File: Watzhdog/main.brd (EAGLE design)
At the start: 100 x 80 mm, 42 parts, among them CN1 MICROUSB(MC-5F-02), IC1 C8051F381-GM, IC3 N25Q512A, IC6 MPU-9250, U1 MCP73831, U2 TPS61201

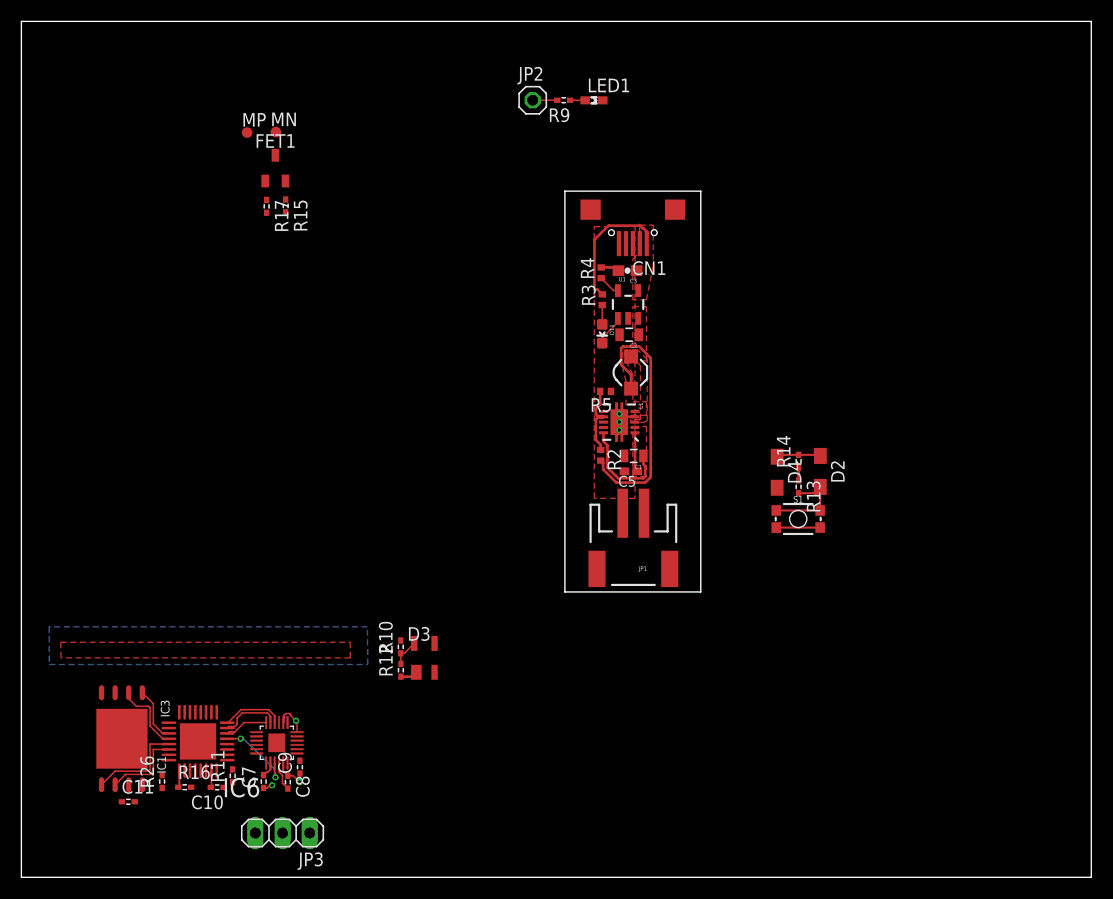
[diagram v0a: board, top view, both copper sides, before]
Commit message: Modified curcuit as a 2-layer board
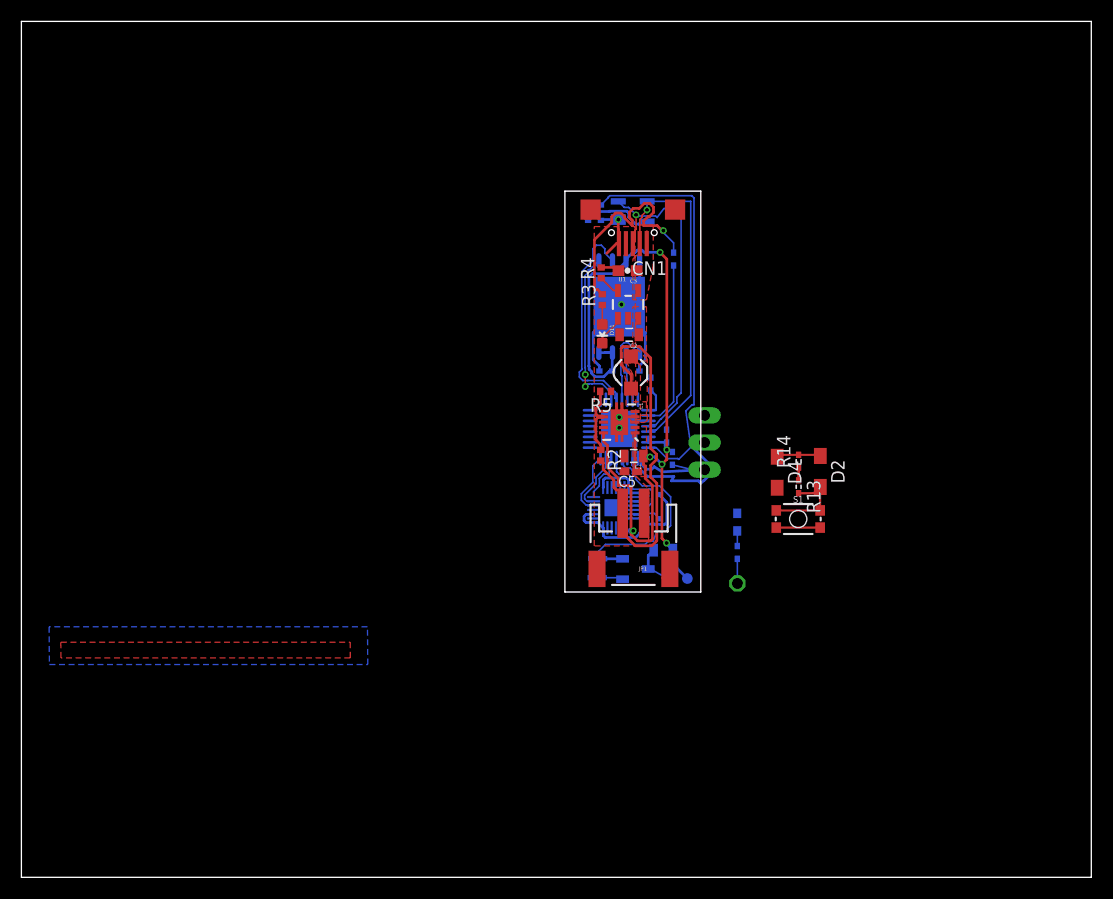
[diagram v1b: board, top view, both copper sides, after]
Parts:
- added C4: 22uF, CH_passive:0805
- added R1: 1k (Optional), reg,cap:1005
- moved IC3 61.6 mm to (55.9, 53.3), flipped to the bottom
- moved C11 60.1 mm to (54.6, 47.3), flipped to the bottom, turned to 180 degrees
- moved MP 58.6 mm to (62.2, 27.9), flipped to the bottom, turned to 90 degrees
- moved R26 58.4 mm to (57.2, 47.3), flipped to the bottom, turned to 0 degrees
- moved R16 57.6 mm to (58.8, 46.1), flipped to the bottom, turned to 90 degrees
- moved MN 55.5 mm to (60.3, 28.0), flipped to the bottom, turned to 90 degrees
- moved JP3 53.7 mm to (63.9, 40.6), flipped to the bottom, turned to 270 degrees
- moved C10 53.3 mm to (60.3, 41.2), flipped to the bottom, turned to 270 degrees
- moved R11 50.7 mm to (60.8, 39.2), flipped to the bottom
- moved FET1 50.4 mm to (57.4, 28.8), flipped to the bottom, turned to 90 degrees
- moved JP2 49.0 mm to (66.9, 27.5), flipped to the bottom, turned to 90 degrees
- moved IC1 49.0 mm to (55.9, 41.9), flipped to the bottom, turned to 0 degrees
- moved R17 46.5 mm to (53.8, 28.0), flipped to the bottom, turned to 0 degrees
- moved D3 46.0 mm to (57.1, 62.2), flipped to the bottom, turned to 90 degrees
- moved R12 45.8 mm to (53.6, 61.4), flipped to the bottom, turned to 0 degrees
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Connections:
- net N$10: now also C4.2
- net N$7: now also R1.P$1
- net VBUS: now also R1.P$2
- net VCC: now also C4.1
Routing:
- net VCC: track 12.4 -> 90.7 mm, vias 0 -> 6
- net DGND: track 14.5 -> 55.9 mm, vias 6 -> 4
- net N$18: track 0.00 -> 37.8 mm
- net D+: track 0.00 -> 32.0 mm, vias 0 -> 1
- net D-: track 0.00 -> 31.8 mm, vias 0 -> 1
- net PWM: track 0.00 -> 20.3 mm
- net VBUS: track 15.8 -> 33.6 mm, vias 0 -> 1
- net N$7: track 0.00 -> 15.6 mm
- net C2D: track 0.00 -> 14.3 mm
- net EEPROM_MISO: track 6.86 -> 20.0 mm
- net VBAT: track 28.7 -> 41.1 mm
- net EEPROM_!CS: track 5.17 -> 16.2 mm, vias 0 -> 2
- net C2CK: track 0.00 -> 9.38 mm
- net N$10: track 0.00 -> 3.95 mm
- net EEPROM_SCK: track 7.57 -> 4.41 mm
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
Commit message: Modified circuit
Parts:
- moved C10 0.33 mm to (60.6, 41.3)
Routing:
- net VBUS: track 33.6 -> 23.0 mm, vias 1 -> 2
- net VCC: track 90.7 -> 95.3 mm, vias 6 -> 7
- net DGND: track 55.9 -> 59.5 mm, vias 4 -> 5
- net D+: track 32.0 -> 29.9 mm, vias 1 -> 2
- net D-: track 31.8 -> 30.3 mm, vias 1 -> 3

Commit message: Modified circuit
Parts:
- moved C9 0.65 mm to (57.0, 32.2)
- moved C10 0.64 mm to (60.0, 41.3)
- moved C11 0.64 mm to (54.0, 47.3)
- moved C5 0.64 mm to (56.3, 37.9)
- moved C7 0.64 mm to (58.4, 35.8)
- moved IC1 0.64 mm to (55.2, 41.9)
- moved IC3 0.64 mm to (55.2, 53.3)
- moved L1 0.64 mm to (56.3, 47.2)
- moved R16 0.64 mm to (58.2, 46.1)
- moved U2 0.64 mm to (55.2, 42.5)
- moved C1 0.63 mm to (56.6, 39.4)
- moved C2 0.63 mm to (56.2, 50.7)
- moved C3 0.63 mm to (56.0, 56.7)
- moved C8 0.63 mm to (58.4, 33.5)
- moved D11 0.63 mm to (53.7, 50.8)
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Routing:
- net VBAT: track 41.4 -> 51.1 mm
- net VCC: track 95.3 -> 86.2 mm, vias 7 -> 8
- net DGND: track 59.5 -> 56.7 mm, vias 5 -> 7
- net PWM: track 20.0 -> 22.4 mm
- net C2CK: track 9.26 -> 10.5 mm
- net N$18: track 37.8 -> 39.0 mm
- net C2D: track 14.2 -> 14.9 mm

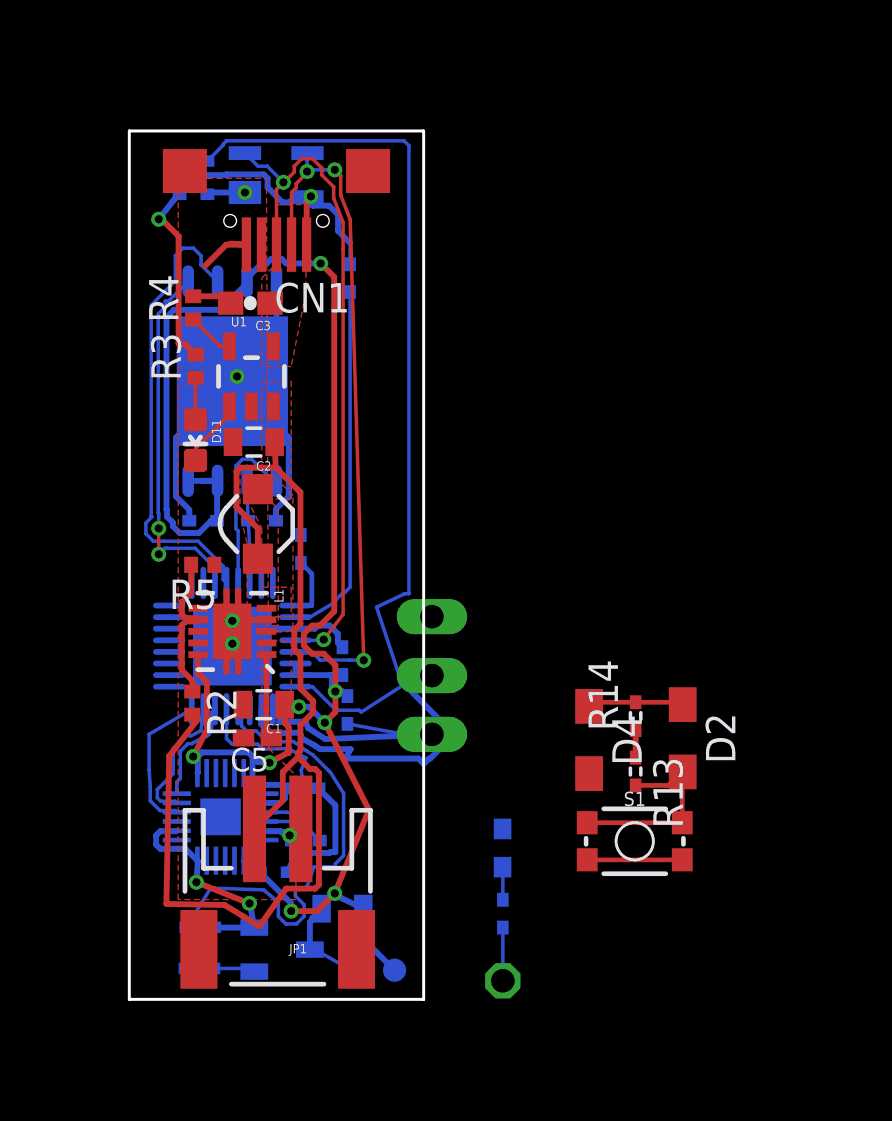
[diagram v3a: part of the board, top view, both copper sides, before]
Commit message: Modified parts position
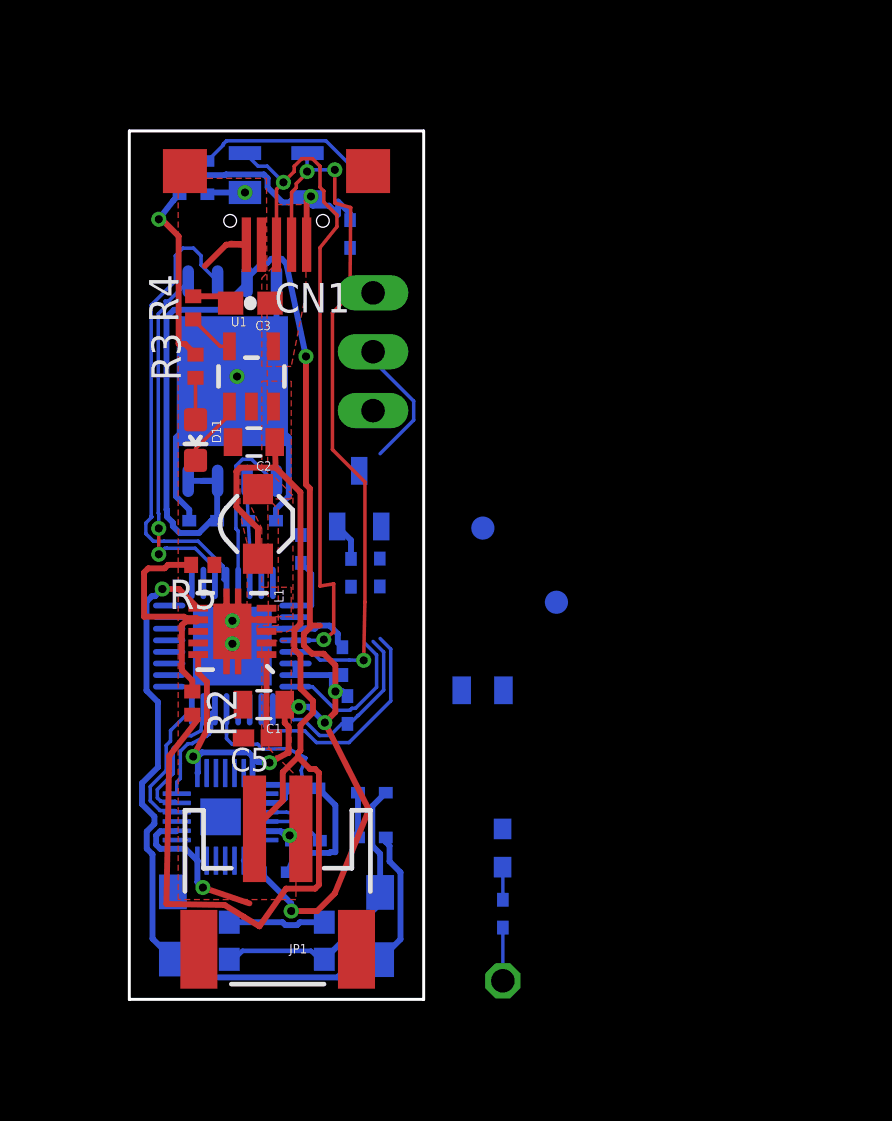
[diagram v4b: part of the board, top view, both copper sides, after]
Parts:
- removed C4: 22uF, CH_passive:0805
- added C6: 22uF, CH_passive:0805
- moved MN 19.9 mm to (66.1, 47.0)
- moved FET1 19.7 mm to (60.7, 48.3), turned to 0 degrees
- moved D4 19.7 mm to (52.7, 29.9), flipped to the bottom, turned to 90 degrees
- moved R17 18.8 mm to (61.6, 45.1), turned to 270 degrees
- moved MP 17.3 mm to (69.2, 43.8)
- moved R15 16.6 mm to (60.4, 45.1), turned to 270 degrees
- moved S1 16.0 mm to (57.2, 29.2), flipped to the bottom, turned to 180 degrees
- moved D2 15.4 mm to (61.6, 29.8), flipped to the bottom, turned to 90 degrees
- moved JP3 14.2 mm to (61.3, 54.6)
- moved R14 12.5 mm to (61.3, 33.7), flipped to the bottom, turned to 180 degrees
- moved R13 11.4 mm to (61.3, 35.6), flipped to the bottom, turned to 180 degrees
- moved R1 1.91 mm to (60.3, 59.7)
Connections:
- net DGND: now also C6.2
- net N$10: no longer C4.2
- net VCC: now also C6.1; no longer C4.1
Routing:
- net N$6: track 4.14 -> 35.0 mm, vias 0 -> 1
- net N$18: track 39.0 -> 14.3 mm
- net PWM: track 22.4 -> 0.00 mm
- net N$7: track 15.6 -> 0.00 mm
- net VCC: track 86.2 -> 79.7 mm, vias 8 -> 7
- net N$11: track 8.56 -> 13.0 mm
- net N$10: track 3.95 -> 0.00 mm
- net UVLO: track 6.95 -> 10.3 mm
- net C2CK: track 10.5 -> 8.36 mm
- net N$8: track 1.83 -> 0.00 mm
- net D-: track 29.9 -> 31.1 mm
- net C2D: track 14.9 -> 15.9 mm
- net D+: track 29.5 -> 30.4 mm
- net VBUS: track 22.9 -> 22.1 mm
- net DGND: vias 7 -> 6

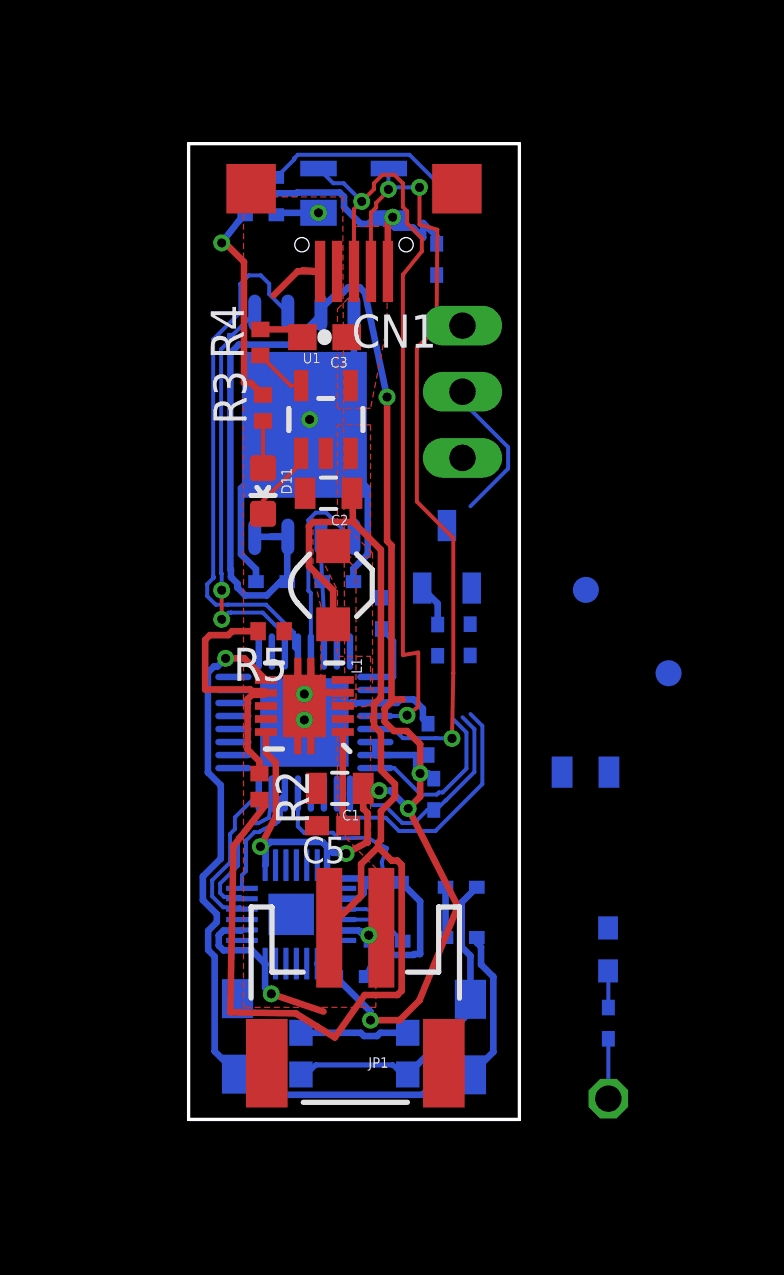
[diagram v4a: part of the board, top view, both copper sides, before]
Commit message: Modified parts position
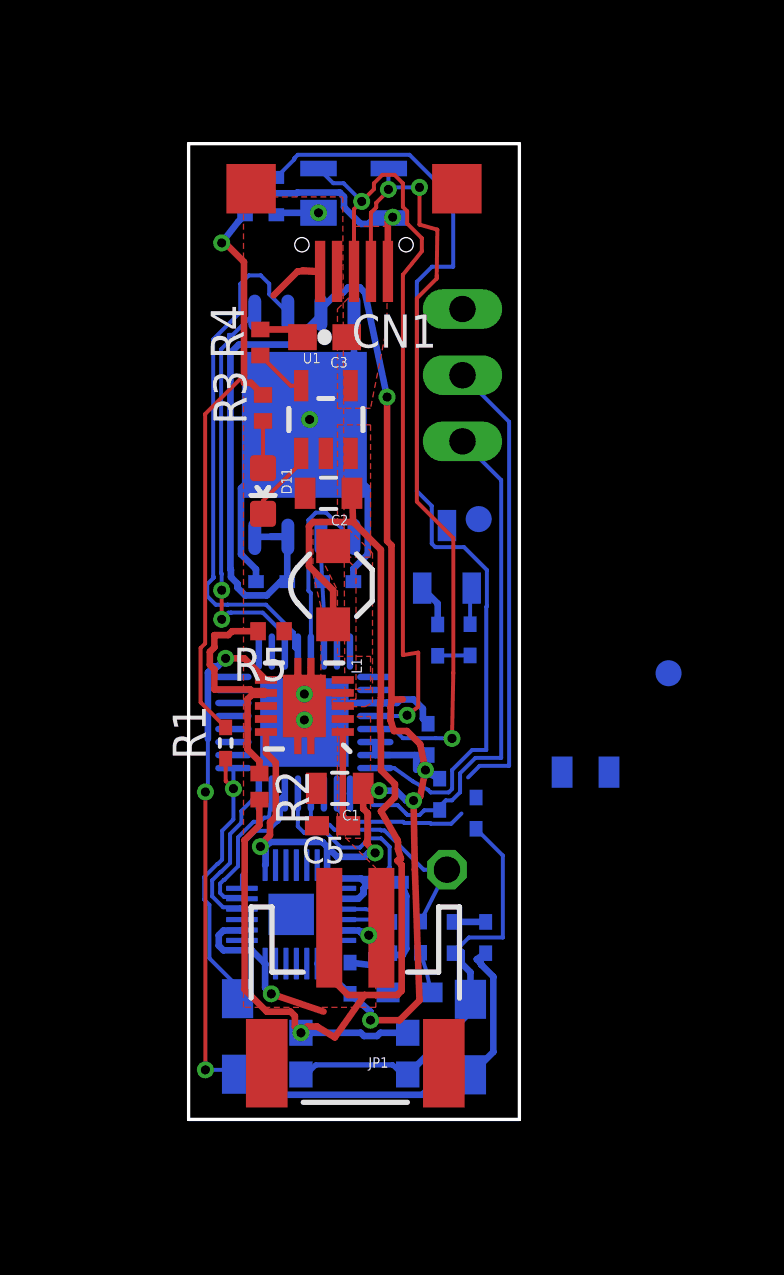
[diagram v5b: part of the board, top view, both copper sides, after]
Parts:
- moved R1 20.3 mm to (52.2, 41.1), flipped to the top
- moved JP2 10.8 mm to (60.7, 36.3)
- moved R16 8.49 mm to (61.8, 38.4), turned to 270 degrees
- moved R9 7.93 mm to (59.7, 33.7), turned to 90 degrees
- moved LED1 7.80 mm to (59.3, 31.5), turned to 0 degrees
- moved MN 4.93 mm to (61.9, 49.7)
- moved R13 1.95 mm to (61.0, 33.7), turned to 270 degrees
- moved R14 0.94 mm to (62.2, 33.7), turned to 270 degrees
- moved JP3 0.63 mm to (61.3, 55.2)
- moved R11 0.23 mm to (60.4, 39.2)
- moved C8 0.20 mm to (58.6, 33.7), turned to 90 degrees
- moved C9 0.07 mm to (57.0, 32.1), turned to 270 degrees
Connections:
- net N$15: now also IC1.12; no longer IC1.11
- net N$5: now also IC1.11; no longer IC1.1
- net N$7: now also IC1.17; no longer IC1.2
- net PWM: now also IC1.32; no longer IC1.12
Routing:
- net N$18: track 14.3 -> 37.6 mm
- net C2CK: track 8.36 -> 20.4 mm
- net VBUS: track 22.1 -> 33.6 mm
- net N$7: track 0.00 -> 11.1 mm, vias 0 -> 1
- net C2D: track 15.9 -> 23.3 mm
- net N$15: track 2.30 -> 9.20 mm
- net N$11: track 13.0 -> 17.3 mm
- net N$5: track 2.74 -> 0.00 mm
- net VBAT: track 51.2 -> 49.6 mm, vias 0 -> 1
- net N$8: track 0.00 -> 1.41 mm
- net PWM: track 0.00 -> 1.30 mm
- net DGND: track 56.7 -> 57.9 mm
- net N$6: track 35.0 -> 34.5 mm, vias 1 -> 3
- net IMU_MISO: track 8.91 -> 9.45 mm

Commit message: Zero airwire
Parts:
- moved C6 12.6 mm to (59.7, 50.9)
- moved MP 10.4 mm to (61.9, 51.2)
- moved R16 0.98 mm to (61.0, 37.9), turned to 180 degrees
- moved IC1 0.64 mm to (55.2, 42.5)
- moved JP3 0.64 mm to (61.3, 55.9)
- moved C10 0.63 mm to (60.0, 41.9)
- moved C11 0.63 mm to (54.0, 48.0)
- moved FET1 0.63 mm to (60.7, 47.6)
- moved IC3 0.63 mm to (55.2, 54.0)
- moved MN 0.63 mm to (61.9, 49.1)
- moved R11 0.63 mm to (60.4, 39.8)
- moved R15 0.63 mm to (60.4, 44.4)
- moved R17 0.63 mm to (61.6, 44.5)
- moved R26 0.63 mm to (56.5, 48.0)
- moved JP2 0.27 mm to (60.8, 36.0)
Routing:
- net VCC: track 80.0 -> 86.6 mm, vias 7 -> 8
- net N$5: track 0.00 -> 5.50 mm
- net PWM: track 1.30 -> 5.26 mm
- net N$18: track 37.6 -> 40.7 mm
- net D+: track 30.4 -> 32.8 mm
- net N$11: track 17.3 -> 19.4 mm
- net C2D: track 23.3 -> 25.0 mm
- net N$10: track 0.00 -> 1.32 mm
- net DGND: track 57.9 -> 59.0 mm
- net N$15: track 9.20 -> 10.1 mm
- net N$6: track 34.5 -> 35.4 mm
- net UVLO: track 9.85 -> 9.06 mm
- net IMU_MISO: track 9.45 -> 10.1 mm
- net N$7: track 11.1 -> 11.7 mm
- net IMU_MOSI: track 4.62 -> 5.17 mm
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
